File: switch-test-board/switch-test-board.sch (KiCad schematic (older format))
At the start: 1 part, among them U1 RPI4CM

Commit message: Sch. update.
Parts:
- added U? (x3): KSZ9477S, kicad-lib:128-TQFP-EP, symbol kicad-lib:KSZ9477S
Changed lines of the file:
@@
+	1    0    0    -1
+$EndComp
+$Comp
+L kicad-lib:KSZ9477S U?
+U 1 1 6061AA85
+P 6900 7300
+F 0 "U?" H 6975 9865 50  0000 C CNN
+F 1 "KSZ9477S" H 6975 9774 50  0000 C CNN
+F 2 "kicad-lib:128-TQFP-EP" H 6900 7300 50  0001 C CNN
+F 3 "" H 6350 6600 50  0001 C CNN
+	1    6900 7300
+	1    0    0    -1
+$EndComp
+$Comp
+L kicad-lib:KSZ9477S U?
+U 2 1 6061D2BA
+P 7400 11200
+F 0 "U?" H 7678 11196 50  0000 L CNN
+F 1 "KSZ9477S" H 7678 11105 50  0000 L CNN
+F 2 "kicad-lib:128-TQFP-EP" H 7400 11200 50  0001 C CNN
+F 3 "" H 6850 10500 50  0001 C CNN
+	2    7400 11200
+	1    0    0    -1
+$EndComp
+$Comp
+L kicad-lib:KSZ9477S U?
+U 3 1 60622016
+P 10000 12500
+F 0 "U?" H 9975 14365 50  0000 C CNN
+F 1 "KSZ9477S" H 9975 14274 50  0000 C CNN
+F 2 "kicad-lib:128-TQFP-EP" H 10000 12500 50  0001 C CNN
+F 3 "" H 9450 11800 50  0001 C CNN
+	3    10000 12500
 	1    0    0    -1
 $EndComp

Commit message: Added KSZ Switch IC Decoupling and Port Leds.
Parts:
- added C1, C?: 1uF, Capacitor_SMD:C_0402_1005Metric, symbol Device:C_Small
- added C10, C2, C3, C4, C5, C6, C7, C8, C9, C? (x23): 0.1uF, Capacitor_SMD:C_0402_1005Metric, symbol Device:C_Small
- added D? (x5): 150060GS75000, LED:LED-0603, symbol Device:LED_Small
- added D? (x5): 150060RS75000, LED:LED-0603, symbol Device:LED_Small
- added FB?: BLM18EG221SN1D, kicad-lib:ferrite-blm18, symbol Device:Ferrite_Bead_Small
- added R? (x10): 1K, Resistor_SMD:R_0402_1005Metric, symbol Device:R_Small_US
- gave numbers to parts that had none: 1
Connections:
- net LED5_0: now reaches U2.102 (LED5_0)
- net LED5_0: now also R?.1
- net LED5_1: now reaches U2.103 (LED5_1)
- net LED5_1: now also R?.1
- net LED1_0: now reaches U2.105 (LED1_0)
- net LED1_0: now also R?.1
- net LED1_1: now reaches U2.106 (LED1_1)
- net LED1_1: now also R?.1
- net LED4_0: now reaches U2.85 (LED4_0)
- net LED4_0: now also R?.1
- net LED4_1: now reaches U2.86 (LED4_1)
- net LED4_1: now also R?.1
- net LED3_0: now reaches U2.88 (LED3_0)
- net LED3_0: now also R?.1
- net LED3_1: now reaches U2.89 (LED3_1)
- net LED3_1: now also R?.1
- net LED2_0: now reaches U2.91 (LED2_0)
- net LED2_0: now also R?.1
- net LED2_1: now reaches U2.92 (LED2_1)
- net LED2_1: now also R?.1
- net AVDDH_2V5: now reaches U2.10 (AVDDH)
- net AVDDH_2V5: now also U2.111 (AVDDH), U2.122 (AVDDH), U2.128 (AVDDH), U2.22 (AVDDH), U2.33 (AVDDH), U2.44 (AVDDH), C?.1, C?.1, C?.1, C?.1, C?.1, C?.1, C?.1
- net +1V2: now reaches U2.104 (DVDDL)
- net +1V2: now also U2.11 (DVDDL), U2.110 (DVDDL), U2.23 (DVDDL), U2.45 (DVDDL), U2.56 (DVDDL), U2.66 (DVDDL), U2.70 (DVDDL), U2.87 (DVDDL), C?.1, C?.1, C?.1, C?.1, C?.1, C?.1, C?.1, C?.1, C?.1, C?.1
- net GND: now reaches U2.107 (GND)
- net GND: now also U2.109 (GND), U2.123 (GND), U2.129 (EPAD), U2.46 (GND), U2.47 (GND), U2.69 (GND), U2.75 (GND), U2.77 (GND), U2.80 (GND), C1.2, C10.2, C2.2, C3.2, C4.2, C5.2, C6.2, C7.2, C8.2, C9.2, C?.2, C?.2, C?.2, C?.2, C?.2, C?.2, C?.2, C?.2, C?.2, C?.2, C?.2, C?.2, C?.2, C?.2, C?.2, C?.2, C?.2, C?.2, C?.2, C?.2, C?.2, C?.2, C?.2, C?.2
- net AVDDL_1V2: now reaches U2.114 (AVDDL)
- net AVDDL_1V2: now also U2.119 (AVDDL), U2.124 (AVDDL), U2.14 (AVDDL), U2.19 (AVDDL), U2.3 (AVDDL), U2.30 (AVDDL), U2.36 (AVDDL), U2.41 (AVDDL), C1.1, C10.1, C2.1, C3.1, C4.1, C5.1, C6.1, C7.1, C8.1, C9.1
- net +3V3: now reaches U2.61 (VDDIO)
- net +3V3: now also U2.68 (VDDIO), U2.99 (VDDIO), C?.1, C?.1, C?.1, D?.2 (A), D?.2 (A), D?.2 (A), D?.2 (A), D?.2 (A), D?.2 (A), D?.2 (A), D?.2 (A), D?.2 (A), D?.2 (A)
- net VDDLS_1V2: now reaches U2.71 (VDDLS)
- net VDDLS_1V2: now also U2.84 (VDDLS), C?.1, C?.1
- net VDDHS_2V5: now reaches U2.72 (VDDHS)
- net VDDHS_2V5: now also U2.83 (VDDHS), C?.1, C?.1
- new net: D?.1 (K), R?.2 (x10)
- no-connect marks 0 -> 1
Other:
- moved on the sheet: U1B, U1C, U1D, U1F, U2A, U2B, U2C

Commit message: Updated Schematic.
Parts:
- added C1, C2: 15pF, Capacitor_SMD:C_0402_1005Metric, symbol Device:C_Small
- added C10, C3, C4, C45, C47, C49, C5, C6, C7, C8, C9: 10uF, Capacitor_SMD:C_0603_1608Metric, symbol Device:C_Small
- added C46, C48, C50, C? (x8): 0.1uF, Capacitor_SMD:C_0402_1005Metric, symbol Device:C_Small
- added D? (x2): 150060RS75000, LED_SMD:LED_0603_1608Metric, symbol Device:LED_Small
- added D?: 150060GS75000, LED_SMD:LED_0603_1608Metric, symbol Device:LED_Small
- added FB1, FB3, FB4, FB5, FB6, FB7: BLM18EG221SN1D, kicad-lib:ferrite-blm18, symbol Device:Ferrite_Bead_Small
- added J1: 1367073-1, kicad-lib:SFP_with_Cage, symbol kicad-lib:1367073-1
- added J3: 2011-2X10G00SD025B, Connector_PinHeader_2.54mm:PinHeader_2x10_P2.54mm_Vertical, symbol Connector_Generic:Conn_02x10_Odd_Even
- added R1: 6.04K %1, Resistor_SMD:R_0402_1005Metric, symbol Device:R_Small_US
- added R10: 10K_DNP, Resistor_SMD:R_0402_1005Metric, symbol Device:R_Small_US
- added R11, R27: 4.7K, Resistor_SMD:R_0402_1005Metric, symbol Device:R_Small_US
- added R12, R13, R14, R15, R16, R37, R38: 10K, Resistor_SMD:R_0402_1005Metric, symbol Device:R_Small_US
- added R2: 191 %1, Resistor_SMD:R_0402_1005Metric, symbol Device:R_Small_US
- added R28, R29, R30, R31, R32, R33, R34: 750R, Resistor_SMD:R_0402_1005Metric, symbol Device:R_Small_US
- added R3, R35, R4, R5, R6, R7, R8, R9: 22R, Resistor_SMD:R_0402_1005Metric, symbol Device:R_Small_US
- added R36, R? (x3): 1K, Resistor_SMD:R_0402_1005Metric, symbol Device:R_Small_US
- added SW1: PTS645SM43SMTR92 LFS, Button_Switch_SMD:SW_SPST_PTS645, symbol Switch:SW_Push
- added TP1: TestPoint_Small, TestPoint:TestPoint_Pad_D1.0mm, symbol Connector:TestPoint_Small
- added U3: MIC826TYMT, Package_DFN_QFN:MLF-6-1EP_1.6x1.6mm_P0.5mm_EP0.5x1.26mm, symbol kicad-lib:MIC826TYMT
- added Y1: ABM8G-25.000MHZ-B4Y-T, Crystal:Crystal_SMD_Abracon_ABM8G-4Pin_3.2x2.5mm, symbol Device:Crystal_GND24_Small
- D1, D10, D2, D3, D4, D5, D6, D7, D8, D9: renamed from D?; footprint LED:LED-0603 -> LED_SMD:LED_0603_1608Metric
- gave numbers to parts that had none: 35
- renumbered C1 to C11, C2 to C13, C3 to C15, C4 to C17, C5 to C20, C6 to C23, C7 to C26, C8 to C29, C9 to C32, C10 to C35
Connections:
- net labels added: 2227302-1, GRXCK, GRXCTL, GRXD0, GRXD1, GRXD2, GRXD3, GTXCK, GTXCTL, GTXD0, GTXD1, GTXD2, GTXD3, IBA_EN, INTRP_N, KSZ_RESETN, MISO, MOSI, P1_TXRX_A_M, P1_TXRX_A_P, P1_TXRX_B_M, P1_TXRX_B_P, P1_TXRX_C_M, P1_TXRX_C_P, P1_TXRX_D_M, P1_TXRX_D_P, P2_TXRX_A_M, P2_TXRX_A_P, P2_TXRX_B_M, P2_TXRX_B_P, P2_TXRX_C_M, P2_TXRX_C_P, P2_TXRX_D_M, P2_TXRX_D_P, PME_N, RPI_ETH_LED1, RPI_ETH_LED2, RPI_ETH_LED3, RPI_ETH_P0_N, RPI_ETH_P0_P, RPI_ETH_P1_N, RPI_ETH_P1_P, RPI_ETH_P2_N, RPI_ETH_P2_P, RPI_ETH_P3_N, RPI_ETH_P3_P, SCLK, SCS, SFP_I2C_SCL, SFP_I2C_SDA, SFP_LOS, SFP_RATE_SEL, SFP_TX_DIS, SFP_TX_FAULT, SW_RESETN, SYN_CLKO, S_RX7_M, S_RX7_P, S_TX7_M, S_TX7_P, VCC_SFP_R, VCC_SFP_T
- wire segments 248 -> 529
- no-connect marks 1 -> 11
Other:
- note added: "For Jumper: \nQPC02SXGN-RC"
- note added: "GRXD0:\nIBA:\nLED2_0:\nLED4_0:\nLED1_0:\nLED1_1:\nLED2_1:\nLED4_1:\nLED5_1:\n"
- note added: "KSZ CONFIG STRAP"
- note added: "KSZ DECOUPLING"
- note added: "KSZ INTERFACES"
- note added: "KSZ PORT LEDS"
- note added: "KSZ RESET"
- note added: "KSZ SGMII SFP"
- note added: "[Closed]\nRGMII: 1000 Mb/s\nIBA off\n1000B-T master or 10/100 MDI\nEnable AN or 100B-TX\nQuiet-WIRE off\nFlow control on\nNormal link up\nSPI\nStart switch\n"
- note added: "[Open]\nRGMII: 100 Mb/s\nIBA enabled\n1000B-T slave or 10/100 MDI-X\nDisable AN or 1000B-T\nQuiet-WIRE on\nFlow control off\nFast link up\nI2C\nDon't start switch\n"
- moved on the sheet: C11, C12, C13, C14, C15, C16, C17, C18, C19, C20, C21, C22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

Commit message: Added PCIe x1 to NVMe adapter.
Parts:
- removed unit 4 of U1
- added R?: 10K, Resistor_SMD:R_0402_1005Metric, symbol Device:R_Small_US
- added TP? (x2): TestPoint, symbol Connector:TestPoint
- added U?: piSlice-PCIe-X1-Conn, kicad-lib:10018783-10200TLF, symbol kicad-lib:piSlice-PCIe-X1-Conn
- added U?: piSlice-PCIe-X1-Edge, kicad-lib:piSlice_PCIexpress_x1, symbol kicad-lib:piSlice-PCIe-X1-Edge
- added U?: MDT420M02001, kicad-lib:M.2_Amphenol_MDT_2280, symbol kicad-lib:MDT420M02001
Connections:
- net labels added: RPI_PCIe_CLK_N, RPI_PCIe_CLK_P, RPI_PCIe_CLK_nREQ, RPI_PCIe_RX_N, RPI_PCIe_RX_P, RPI_PCIe_TX_N, RPI_PCIe_TX_P, RPI_PCIe_nRST
- wire segments 529 -> 592
- no-connect marks 11 -> 43
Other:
- note added: "1-PCIE Power Supply\n2-Pislice Edge Connector Ethernet\n3-Pislice x1 Connector Ethernet\n4-Power Inputs\n"
- note added: "M.2 SSD Connector"
- note added: "M.2 SSD Power"
- note added: "Power"
- note added: "RPI PCIe x1"
- note added: "piSlice Edge Ethernet"
- note added: "piSlice X1 Ethernet"
- moved on the sheet: U1B

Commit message: Schematic completed.
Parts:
- removed C? (x8): 0.1uF, Capacitor_SMD:C_0402_1005Metric, symbol Device:C_Small
- added C? (x27): 0.1uF, Capacitor_SMD:C_0402_1005Metric, symbol Device:C_Small
- added C? (x21): 10uF, Capacitor_SMD:C_0603_1608Metric, symbol Device:C_Small
- added D?: 150060RS75000, LED_SMD:LED_0603_1608Metric, symbol Device:LED_Small
- added D?: SMAJ5.0CA-TR, Diode_SMD:D_SMA, symbol Device:D_TVS
- added H?: VIN+, MountingHole:MountingHole_3.2mm_M3_Pad, symbol Mechanical:MountingHole_Pad
- added H?: VIN-, MountingHole:MountingHole_3.2mm_M3_Pad, symbol Mechanical:MountingHole_Pad
- added J?: 2011-2X10G00SD025B, Connector_PinHeader_2.54mm:PinHeader_2x10_P2.54mm_Vertical, symbol Connector_Generic:Conn_02x10_Odd_Even
- added J?: USB_B_Micro, Connector_USB:USB_Micro-B_GCT_USB3076-30-A, symbol Connector:USB_B_Micro
- added R?: 0R_DNP, Resistor_SMD:R_0402_1005Metric, symbol Device:R_Small_US
- added R?: 0R, Resistor_SMD:R_0402_1005Metric, symbol Device:R_Small_US
- added R? (x2): 4.7K, Resistor_SMD:R_0402_1005Metric, symbol Device:R_Small_US
- added R?: 1K, Resistor_SMD:R_0402_1005Metric, symbol Device:R_Small_US
- added R?: 2.2K, Resistor_SMD:R_0402_1005Metric, symbol Device:R_Small_US
- added R?: 2.2K_DNP, Resistor_SMD:R_0402_1005Metric, symbol Device:R_Small_US
- added R?: 56K, Resistor_SMD:R_0402_1005Metric, symbol Device:R_Small_US
- added R? (x3): 10K, Resistor_SMD:R_0402_1005Metric, symbol Device:R_Small_US
- added R?: 40.2K, Resistor_SMD:R_0402_1005Metric, symbol Device:R_Small_US
- added R?: 24K, Resistor_SMD:R_0402_1005Metric, symbol Device:R_Small_US
- added TP? (x5): TestPoint, TestPoint:TestPoint_Pad_D1.0mm, symbol Connector:TestPoint
- added U? (x3): LD39200PUR, Package_DFN_QFN:DFN-6-1EP_3x3mm_P0.95mm_EP1.7x2.6mm, symbol kicad-lib:LD39200PUR
- added U?: LM1085ISX-3.3/NOPB, Package_TO_SOT_SMD:TO-263-3_TabPin2, symbol Regulator_Linear:LM1085-3.3
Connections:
- net labels added: 3V3_PCIE, EEPROM_nWP, GLOBAL_EN, LED_Activity, LED_PWR, P3_TXRX_A_M, P3_TXRX_A_P, P3_TXRX_B_M, P3_TXRX_B_P, P3_TXRX_C_M, P3_TXRX_C_P, P3_TXRX_D_M, P3_TXRX_D_P, RPI_1V8, RPI_3V3, RPI_UART_RX, RPI_UART_TX, RPI_USB_DM, RPI_USB_DP, RPI_USB_ID, RUN_PG, X1_CON_ETH_P0_N, X1_CON_ETH_P0_P, X1_CON_ETH_P1_N, X1_CON_ETH_P1_P, X1_CON_ETH_P2_N, X1_CON_ETH_P2_P, X1_CON_ETH_P3_N, X1_CON_ETH_P3_P, X1_EDGE_ETH_P0_N, X1_EDGE_ETH_P0_P, X1_EDGE_ETH_P1_N, X1_EDGE_ETH_P1_P, X1_EDGE_ETH_P2_N, X1_EDGE_ETH_P2_P, X1_EDGE_ETH_P3_N, X1_EDGE_ETH_P3_P, nEXTRST, nRPIBOOT
- wire segments 592 -> 826
- no-connect marks 43 -> 47
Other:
- note added: "Cap. Coupling\n"
- note added: "RPI Core"
- note added: "RPI Peripherals"
- note added: "rPI Ethernet"
- note removed: "1-PCIE Power Supply\n2-Pislice Edge Connector Ethernet\n3-Pislice x1 Connector Ethernet\n4-Power Inputs\n"
- note removed: "M.2 SSD Power"
- moved on the sheet: D?, R?, U1A, U1B, U1C, U1F, U?

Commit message: PCB Design planning.
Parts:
- TP7, TP8: renamed from TP?; footprint (none) -> TestPoint:TestPoint_Pad_D1.0mm
- gave numbers to parts that had none: 86
- renumbered C45 to C1, C49 to C22, C46 to C3, C50 to C35, C1 to C36, C2 to C37, C3 to C40, C4 to C42, C5 to C45, C6 to C46, C7 to C52, C8 to C53, C9 to C57, C10 to C58, C11 to C59, C12 to C60, C13 to C61, C14 to C62, C15 to C63, C16 to C64, C17 to C67, C18 to C68, C19 to C69, C20 to C72, C21 to C73, C22 to C74, C23 to C77, C24 to C78, C25 to C79, C47 to C8, C26 to C80, C27 to C81, C28 to C82, C29 to C83, C30 to C84, C31 to C85, C32 to C86, C33 to C87, C34 to C88, C35 to C89, C48 to C9, C36 to C90, C37 to C91, C38 to C92, C39 to C93, C40 to C94, C41 to C95, C42 to C96, C43 to C97, C44 to C98, D5 to D10, D6 to D11, D7 to D12, D8 to D13, D9 to D14, D10 to D15, D1 to D6, D2 to D7, D3 to D8, D4 to D9, FB6 to FB1, FB7 to FB2, FB1 to FB3, FB2 to FB4, FB3 to FB5, FB4 to FB6, FB5 to FB7, J1 to J3, J3 to J4, R1 to R14, R2 to R15, R3 to R16, R4 to R17, R5 to R18, R6 to R19, R7 to R20, R8 to R21, R9 to R22, R10 to R23, R11 to R24, R12 to R25, R13 to R26, R14 to R27, R15 to R28, R16 to R29, R36 to R3, R27 to R32, R28 to R33, R29 to R34, R30 to R35, R31 to R36, R32 to R37, R33 to R38, R34 to R39, R37 to R4, R17 to R40, R18 to R41, R19 to R42, R20 to R43, R21 to R44, R22 to R45, R23 to R46, R24 to R47, R25 to R48, R26 to R49, R38 to R5, R35 to R55, U3 to U9

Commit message: PCB Design Updated.
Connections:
- net labels added: S_RX7_N, S_TX7_N
- net labels removed: S_RX7_M, S_TX7_M
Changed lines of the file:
@@
 	9850 14650 10000 14650
 Text Label 9600 12150 0    50   ~ 0
-S_TX7_M
+S_TX7_N
 Text Label 9600 12250 0    50   ~ 0
 S_TX7_P
 Text Label 9600 12450 0    50   ~ 0
-S_RX7_M
+S_RX7_N
 Text Label 9600 12550 0    50   ~ 0
 S_RX7_P
@@
 	5150 12750 5150 12700
 Text Label 5700 13750 0    50   ~ 0
-S_TX7_M
+S_TX7_N
 Text Label 5700 13650 0    50   ~ 0
 S_TX7_P
 Text Label 5700 14050 0    50   ~ 0
-S_RX7_M
+S_RX7_N
 Text Label 5700 13950 0    50   ~ 0
 S_RX7_P

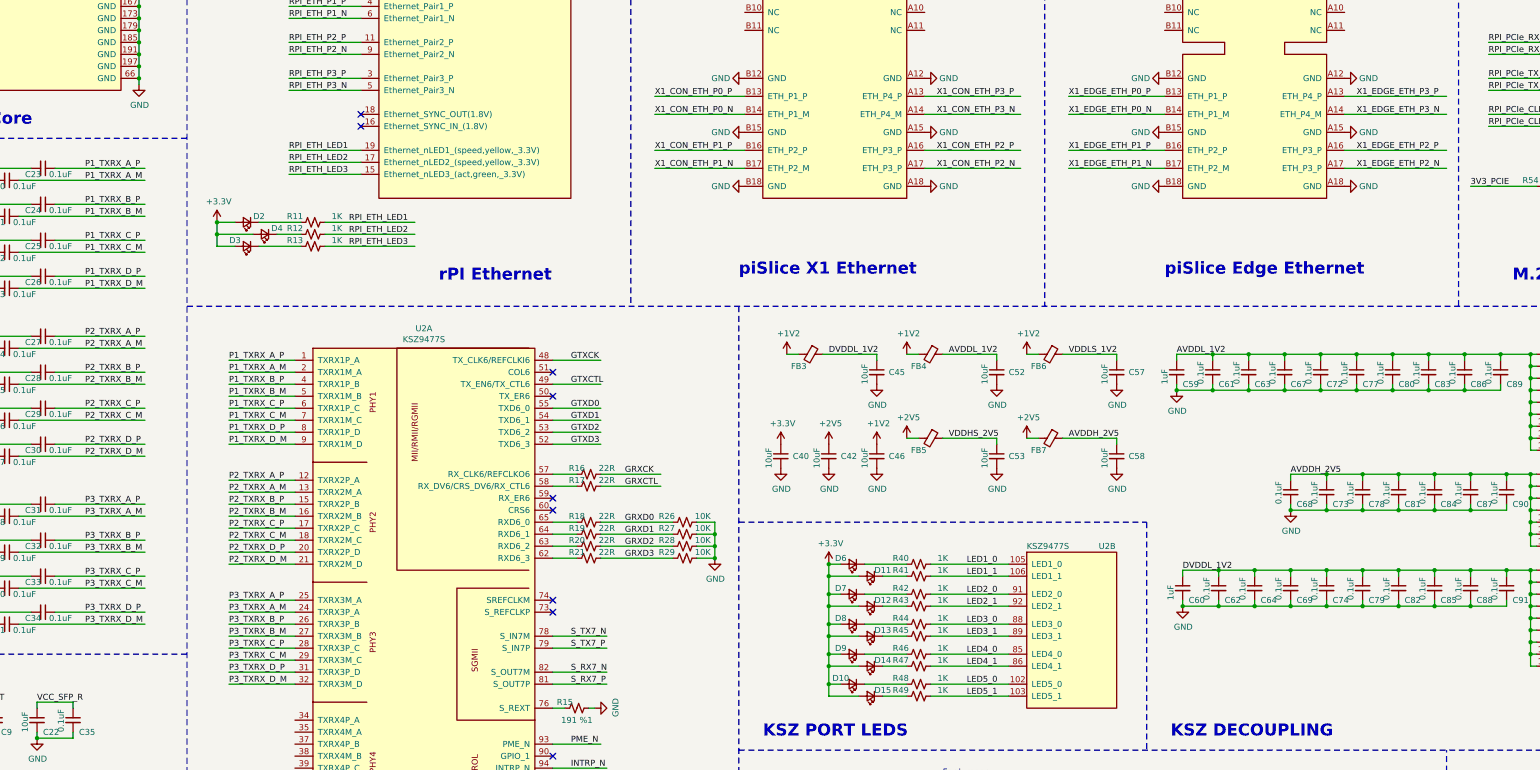
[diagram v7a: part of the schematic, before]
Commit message: Completed routing eth. interfaces.
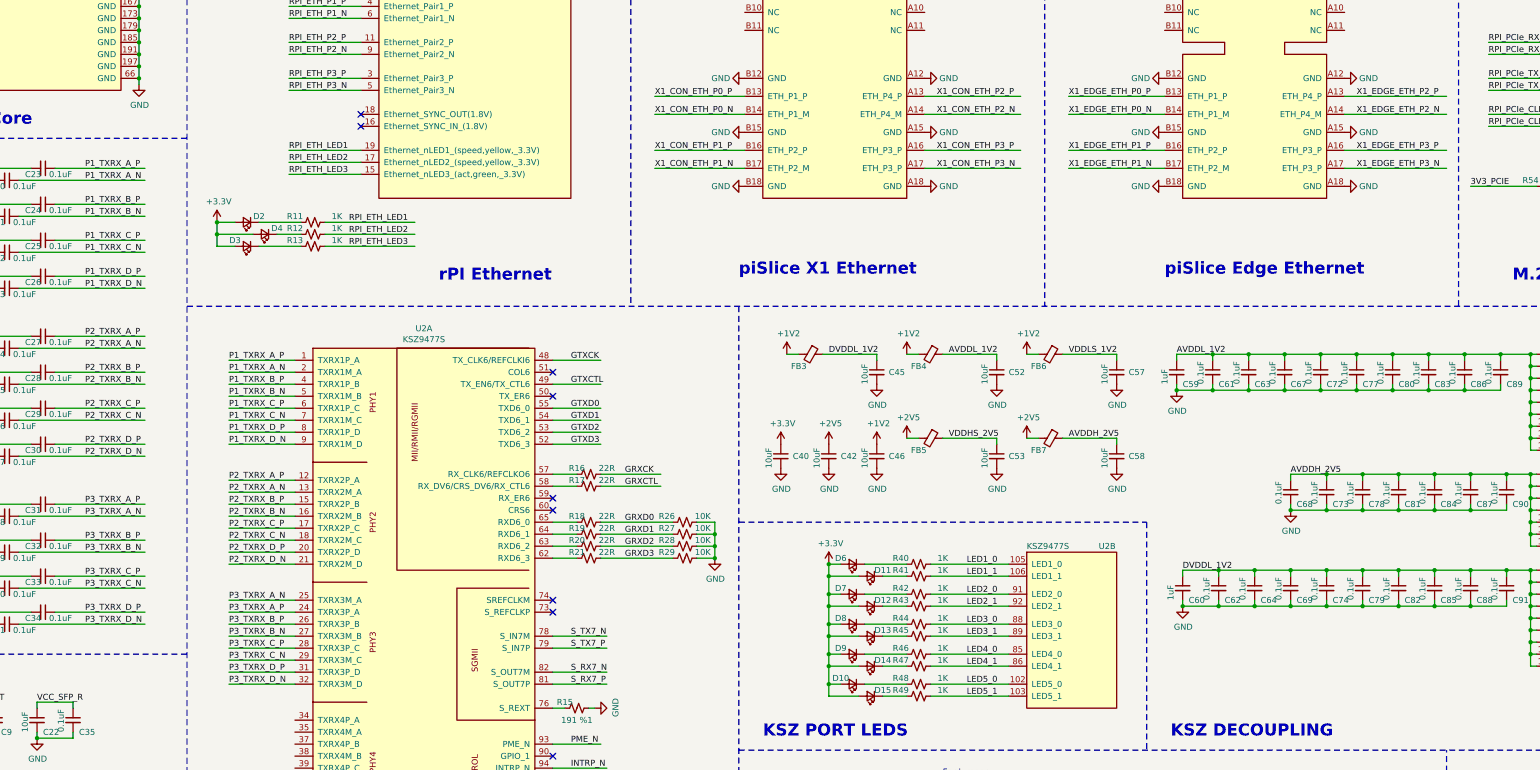
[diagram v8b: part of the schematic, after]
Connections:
- net labels added: P1_TXRX_A_N, P1_TXRX_B_N, P1_TXRX_C_N, P1_TXRX_D_N, P2_TXRX_A_N, P2_TXRX_B_N, P2_TXRX_C_N, P2_TXRX_D_N, P3_TXRX_A_N, P3_TXRX_B_N, P3_TXRX_C_N, P3_TXRX_D_N
- net labels removed: P1_TXRX_A_M, P1_TXRX_B_M, P1_TXRX_C_M, P1_TXRX_D_M, P2_TXRX_A_M, P2_TXRX_B_M, P2_TXRX_C_M, P2_TXRX_D_M, P3_TXRX_A_M, P3_TXRX_B_M, P3_TXRX_C_M, P3_TXRX_D_M
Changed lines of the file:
@@
 P1_TXRX_A_P
 Text Label 6750 9950 0    50   ~ 0
-P1_TXRX_A_M
+P1_TXRX_A_N
 Text Label 6750 10050 0    50   ~ 0
 P1_TXRX_B_P
 Text Label 6750 10150 0    50   ~ 0
-P1_TXRX_B_M
+P1_TXRX_B_N
 Text Label 6750 10250 0    50   ~ 0
 P1_TXRX_C_P
 Text Label 6750 10350 0    50   ~ 0
-P1_TXRX_C_M
+P1_TXRX_C_N
 Text Label 6750 10450 0    50   ~ 0
 P1_TXRX_D_P
 Text Label 6750 10550 0    50   ~ 0
-P1_TXRX_D_M
+P1_TXRX_D_N
 Wire Wire Line
 	7300 9850 6750 9850
@@
 P2_TXRX_A_P
 Text Label 6750 10950 0    50   ~ 0
-P2_TXRX_A_M
+P2_TXRX_A_N
 Text Label 6750 11050 0    50   ~ 0
 P2_TXRX_B_P
 Text Label 6750 11150 0    50   ~ 0
-P2_TXRX_B_M
+P2_TXRX_B_N
 Text Label 6750 11250 0    50   ~ 0
 P2_TXRX_C_P
 Text Label 6750 11350 0    50   ~ 0
-P2_TXRX_C_M
+P2_TXRX_C_N
 Text Label 6750 11450 0    50   ~ 0
 P2_TXRX_D_P
 Text Label 6750 11550 0    50   ~ 0
-P2_TXRX_D_M
+P2_TXRX_D_N
 Wire Wire Line
 	7300 10850 6750 10850
@@
 Wire Wire Line
 	7300 11550 6750 11550
-Text Label 6750 11850 0    50   ~ 0
-P3_TXRX_A_P
 Text Label 6750 11950 0    50   ~ 0
-P3_TXRX_A_M
+P3_TXRX_A_P
+Text Label 6750 11850 0    50   ~ 0
+P3_TXRX_A_N
 Text Label 6750 12050 0    50   ~ 0
 P3_TXRX_B_P
 Text Label 6750 12150 0    50   ~ 0
-P3_TXRX_B_M
+P3_TXRX_B_N
 Text Label 6750 12250 0    50   ~ 0
 P3_TXRX_C_P
 Text Label 6750 12350 0    50   ~ 0
-P3_TXRX_C_M
+P3_TXRX_C_N
 Text Label 6750 12450 0    50   ~ 0
 P3_TXRX_D_P
 Text Label 6750 12550 0    50   ~ 0
-P3_TXRX_D_M
+P3_TXRX_D_N
 Wire Wire Line
 	7300 11850 6750 11850
@@
 P1_TXRX_A_P
 Text Label 5550 8350 0    50   ~ 0
-P1_TXRX_A_M
+P1_TXRX_A_N
 Text Label 5550 8550 0    50   ~ 0
 P1_TXRX_B_P
 Text Label 5550 8650 0    50   ~ 0
-P1_TXRX_B_M
+P1_TXRX_B_N
 Text Label 5550 8850 0    50   ~ 0
 P1_TXRX_C_P
 Text Label 5550 8950 0    50   ~ 0
-P1_TXRX_C_M
+P1_TXRX_C_N
 Text Label 5550 9150 0    50   ~ 0
 P1_TXRX_D_P
 Text Label 5550 9250 0    50   ~ 0
-P1_TXRX_D_M
+P1_TXRX_D_N
 $Comp
 L Device:C_Small C25
@@
 Cap. Coupling\n
 Text Label 5550 12050 0    50   ~ 0
-P3_TXRX_D_M
+P3_TXRX_D_N
 Text Label 5550 11950 0    50   ~ 0
 P3_TXRX_D_P
 Text Label 5550 11750 0    50   ~ 0
-P3_TXRX_C_M
+P3_TXRX_C_N
 Text Label 5550 11650 0    50   ~ 0
 P3_TXRX_C_P
 Text Label 5550 11450 0    50   ~ 0
-P3_TXRX_B_M
+P3_TXRX_B_N
 Text Label 5550 11350 0    50   ~ 0
 P3_TXRX_B_P
 Text Label 5550 11150 0    50   ~ 0
-P3_TXRX_A_M
+P3_TXRX_A_N
 Text Label 5550 11050 0    50   ~ 0
 P3_TXRX_A_P
@@
 $EndComp
 Text Label 5550 10650 0    50   ~ 0
-P2_TXRX_D_M
+P2_TXRX_D_N
 Text Label 5550 10550 0    50   ~ 0
 P2_TXRX_D_P
 Text Label 5550 10350 0    50   ~ 0
-P2_TXRX_C_M
+P2_TXRX_C_N
 Text Label 5550 10250 0    50   ~ 0
 P2_TXRX_C_P
 Text Label 5550 10050 0    50   ~ 0
-P2_TXRX_B_M
+P2_TXRX_B_N
 Text Label 5550 9950 0    50   ~ 0
 P2_TXRX_B_P
 Text Label 5550 9750 0    50   ~ 0
-P2_TXRX_A_M
+P2_TXRX_A_N
 Text Label 5550 9650 0    50   ~ 0
 P2_TXRX_A_P
@@
 Text Label 10300 8250 0    50   ~ 0
 X1_CON_ETH_P1_N
-Text Label 12650 8100 0    50   ~ 0
-X1_CON_ETH_P2_P
-Text Label 12650 8250 0    50   ~ 0
-X1_CON_ETH_P2_N
-Text Label 12650 7650 0    50   ~ 0
-X1_CON_ETH_P3_P
-Text Label 12650 7800 0    50   ~ 0
-X1_CON_ETH_P3_N
 Text Label 13750 7650 0    50   ~ 0
 X1_EDGE_ETH_P0_P
@@
 Text Label 13750 8250 0    50   ~ 0
 X1_EDGE_ETH_P1_N
-Text Label 16150 8100 0    50   ~ 0
-X1_EDGE_ETH_P2_P
-Text Label 16150 8250 0    50   ~ 0
-X1_EDGE_ETH_P2_N
-Text Label 16150 7650 0    50   ~ 0
-X1_EDGE_ETH_P3_P
-Text Label 16150 7800 0    50   ~ 0
-X1_EDGE_ETH_P3_N
 Wire Wire Line
 	14550 7650 13750 7650
@@
 	14550 8250 13750 8250
 Wire Wire Line
-	16050 8100 16900 8100
-Wire Wire Line
-	16050 8250 16900 8250
-Wire Wire Line
-	16050 7800 16900 7800
-Wire Wire Line
-	16050 7650 16900 7650
-Wire Wire Line
 	11050 7650 10300 7650
 Wire Wire Line
@@
 Wire Wire Line
 	11050 8250 10300 8250
-Wire Wire Line
-	12550 8100 13350 8100
-Wire Wire Line
-	12550 8250 13350 8250
-Wire Wire Line
-	12550 7650 13350 7650
-Wire Wire Line
-	12550 7800 13350 7800
 $Comp
 L OLIMEX_Power:GND #PWR030
@@
 	1    0    0    -1
 $EndComp
+Text Label 12650 8100 0    50   ~ 0
+X1_CON_ETH_P3_P
+Text Label 12650 8250 0    50   ~ 0
+X1_CON_ETH_P3_N
+Wire Wire Line
+	12550 8100 13350 8100
+Wire Wire Line
+	12550 8250 13350 8250
+Text Label 12650 7650 0    50   ~ 0
+X1_CON_ETH_P2_P
+Text Label 12650 7800 0    50   ~ 0
+X1_CON_ETH_P2_N
+Wire Wire Line
+	12550 7650 13350 7650
+Wire Wire Line
+	12550 7800 13350 7800
+Text Label 16150 8100 0    50   ~ 0
+X1_EDGE_ETH_P3_P
+Text Label 16150 8250 0    50   ~ 0
+X1_EDGE_ETH_P3_N
+Wire Wire Line
+	16050 8250 16900 8250
+Wire Wire Line
+	16050 8100 16900 8100
+Text Label 16150 7650 0    50   ~ 0
+X1_EDGE_ETH_P2_P
+Text Label 16150 7800 0    50   ~ 0
+X1_EDGE_ETH_P2_N
+Wire Wire Line
+	16050 7650 16900 7650
+Wire Wire Line
+	16050 7800 16900 7800
 $EndSCHEMATC
